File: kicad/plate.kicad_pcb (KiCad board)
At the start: 2 copper layers, 123.5 x 85.3 mm, 22 parts, among them J1 TRRS, SW10 SW_PUSH, SW11 SW_PUSH, SW12 SW_PUSH, SW14 SW_PUSH, SW15 SW_PUSH, SW16 SW_PUSH, SW17 SW_PUSH, SW18 SW_PUSH, SW2 SW_PUSH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

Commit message: Plate build
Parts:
- SW10, SW11, SW12, SW14, SW15, SW16, SW17, SW18, SW2, SW20, SW21, SW3, SW4, SW5, SW6, SW8, SW9: footprint chocs:SW_PG1350_reversible_b2 -> broom:SW_PG1350_cut
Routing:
- net (no net): track 1542.1 -> 0.00 mm, vias 9 -> 0
- removed copper zone on B.Cu, net (none)
- removed copper zone on F.Cu, net (none)

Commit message: Plate ready
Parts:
- removed J1: TRRS, broom:TRRS-PJ-DPB2
- removed RSW1: Val**, foostan:ResetSW
- removed U1: ProMicro, broom:ProMicro_v2
- removed h2 (x2): h2, chocorne:LEGO_HOLE
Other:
- outline, holes or cut-outs redrawn

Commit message: pm cover
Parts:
- added h2: h2, chocorne:LEGO_HOLE, F.Cu at (197.3, 109.0)
- added h2: h2, chocorne:LEGO_HOLE, F.Cu at (212.6, 109.0)
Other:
- board size 123.5 x 85.3 mm -> 126.8 x 85.3 mm
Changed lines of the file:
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@@
     (fp_line (start -7 -7) (end 7 -7) (layer "Edge.Cuts") (width 0.15))
+  )
+  (footprint "chocorne:LEGO_HOLE" (layer "F.Cu")
+    (at 197.322 108.987)
+    (descr "Mounting Hole 2.2mm, no annular, M2")
+    (tags "mounting hole 2.2mm no annular m2")
+    (attr exclude_from_pos_files exclude_from_bom)
+    (fp_text reference "h2" (at 0 -3.2) (layer "F.SilkS") hide
+      (effects (font (size 1 1) (thickness 0.15)))
+    )
+    (fp_text value "h2" (at 0 3.2) (layer "F.Fab")
+      (effects (font (size 1 1) (thickness 0.15)))
+    )
+    (fp_text user "${REFERENCE}" (at 0.3 0) (layer "F.Fab")
+      (effects (font (size 1 1) (thickness 0.15)))
+    )
+    (fp_circle (center 0 0) (end 1.2 0) (layer "Cmts.User") (width 0.15) (fill none))
+    (fp_circle (center 0 0) (end 1.2 0) (layer "F.CrtYd") (width 0.05) (fill none))
+    (pad "h2" thru_hole circle locked (at 0 0) (size 2.4 2.4) (drill 2.2) (layers *.Cu *.Mask))
   )
   (footprint "broom:SW_PG1350_cut" (layer "F.Cu")
@@
     (fp_line (start -7 7) (end 7 7) (layer "Edge.Cuts") (width 0.15))
     (fp_line (start 7 7) (end 7 -7) (layer "Edge.Cuts") (width 0.15))
+  )
+  (footprint "chocorne:LEGO_HOLE" (layer "F.Cu")
+    (at 212.567 108.982)
+    (descr "Mounting Hole 2.2mm, no annular, M2")
+    (tags "mounting hole 2.2mm no annular m2")
+    (attr exclude_from_pos_files exclude_from_bom)
+    (fp_text reference "h2" (at 0 -3.2) (layer "F.SilkS") hide
+      (effects (font (size 1 1) (thickness 0.15)))
+    )
+    (fp_text value "h2" (at 0 3.2) (layer "F.Fab")
+      (effects (font (size 1 1) (thickness 0.15)))
+    )
+    (fp_text user "${REFERENCE}" (at 0.3 0) (layer "F.Fab")
+      (effects (font (size 1 1) (thickness 0.15)))
+    )
+    (fp_circle (center 0 0) (end 1.2 0) (layer "Cmts.User") (width 0.15) (fill none))
+    (fp_circle (center 0 0) (end 1.2 0) (layer "F.CrtYd") (width 0.05) (fill none))
+    (pad "h2" thru_hole circle locked (at 0 0) (size 2.4 2.4) (drill 2.2) (layers *.Cu *.Mask))
   )
   (footprint "broom:SW_PG1350_cut" (layer "F.Cu")
@@
   )
   (gr_arc (start 189.869405 63.084258) (end 190.664405 63.059258) (angle -75.82503188) (layer "Edge.Cuts") (width 0.15))
+  (gr_line (start 194.086 72.697) (end 214.538 72.697) (layer "Edge.Cuts") (width 0.15))
   (gr_line (start 211.234 117.98) (end 211.231003 128.040862) (layer "Edge.Cuts") (width 0.15))
   (gr_line (start 190.669 118) (end 190.664405 63.059258) (layer "Edge.Cuts") (width 0.15))
+  (gr_line (start 194.123 111.275) (end 214.538 111.262) (layer "Edge.Cuts") (width 0.15))
   (gr_line (start 88.127953 83.292666) (end 105.361412 136.251738) (layer "Edge.Cuts") (width 0.15))
+  (gr_line (start 194.086 111.262) (end 194.086 72.697) (layer "Edge.Cuts") (width 0.15))
   (gr_arc (start 155.4857 240.406359) (end 190.039849 62.307342) (angle -30.52241692) (layer "Edge.Cuts") (width 0.15))
   (gr_arc (start 188.968743 128.55) (end 206.239908 142.606113) (angle -40.45049692) (layer "Edge.Cuts") (width 0.15))
@@
   (gr_arc (start 141.689 320.542281) (end 106.709135 136.975628) (angle 18.02701016) (layer "Edge.Cuts") (width 0.15))
   (gr_arc (start 135.189 334.05) (end 165.233781 135.161726) (angle 10.5566717) (layer "Edge.Cuts") (width 0.15))
+  (gr_line (start 214.538 111.262) (end 214.538 72.697) (layer "Edge.Cuts") (width 0.15))
   (gr_arc (start 202.695496 139.738695) (end 201.163167 144.032518) (angle -70.66711935) (layer "Edge.Cuts") (width 0.15))
   (gr_arc (start 106.46079 135.821466) (end 105.361412 136.251738) (angle -80.76911852) (layer "Edge.Cuts") (width 0.15))

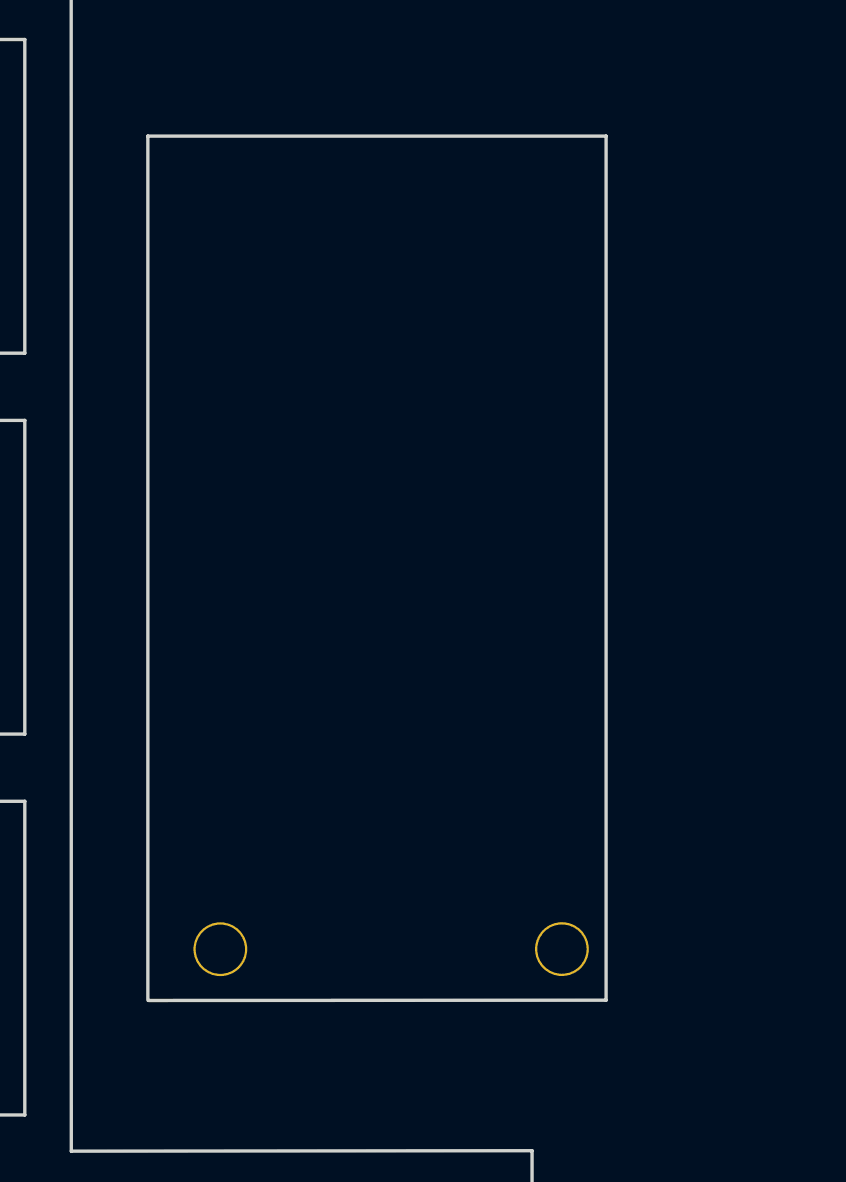
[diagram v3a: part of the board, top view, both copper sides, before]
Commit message: pm cover - mouse bites
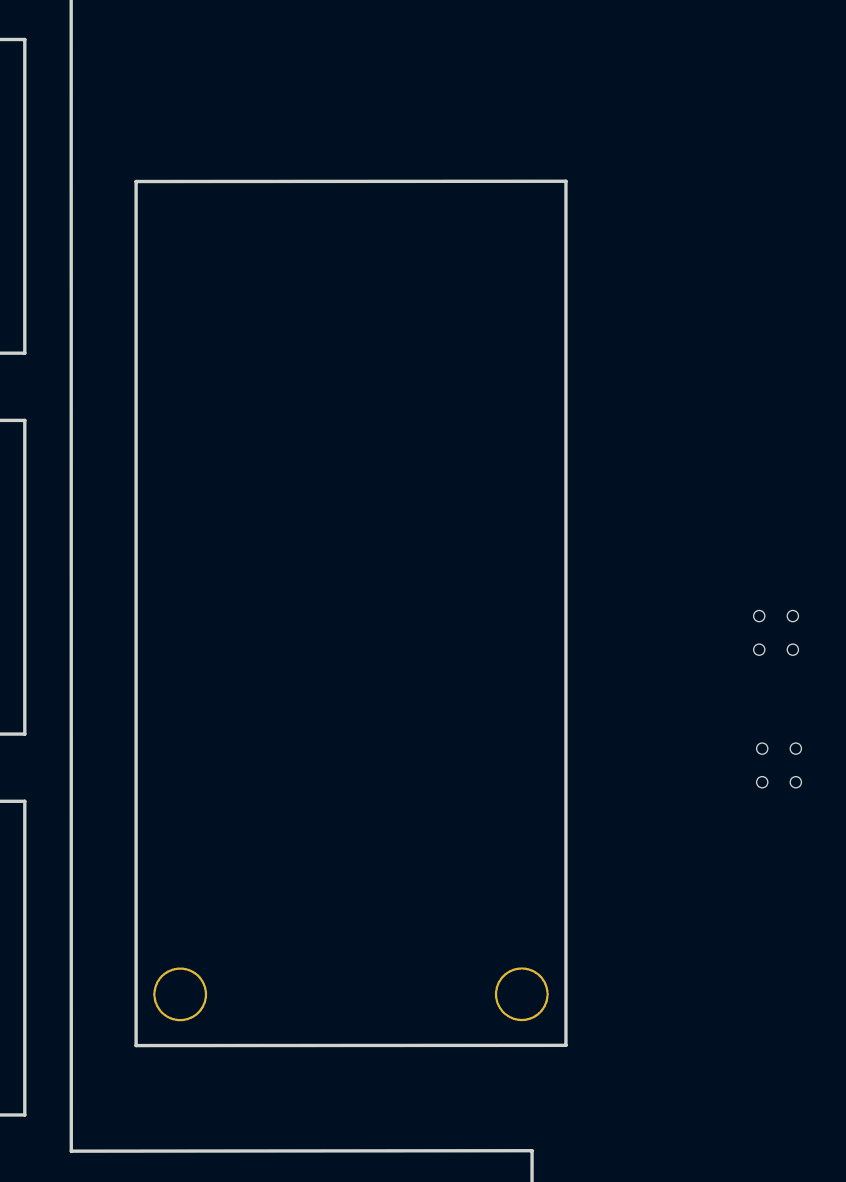
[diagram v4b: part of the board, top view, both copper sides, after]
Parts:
- added REF**: VAL**, broom:mouse-bite-2mm-slot-with-space-for-track, F.Cu at (222.1, 94.9)
- added REF**: VAL**, broom:mouse-bite-2mm-slot-with-space-for-track, F.Cu at (222.3, 100.8)
- moved h2 2.70 mm to (195.5, 111.0)
- moved h2 2.70 mm to (210.8, 111.0)
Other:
- board size 126.8 x 85.3 mm -> 125 x 85.3 mm
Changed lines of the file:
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@@
   )
   (net 0 "")
+  (footprint "broom:mouse-bite-2mm-slot-with-space-for-track" (layer "F.Cu")
+    (at 222.123 94.868 90)
+    (attr exclude_from_pos_files exclude_from_bom)
+    (fp_text reference "REF**" (at 0 -2 90) (layer "F.SilkS") hide
+      (effects (font (size 1 1) (thickness 0.2)))
+    )
+    (fp_text value "VAL**" (at 0 2.1 90) (layer "F.SilkS") hide
+      (effects (font (size 1 1) (thickness 0.2)))
+    )
+    (fp_arc (start -2 0) (end -2 -1) (angle 180) (layer "Dwgs.User") (width 0.1))
+    (fp_arc (start 2 0) (end 2 1) (angle 180) (layer "Dwgs.User") (width 0.1))
+    (fp_circle (center 2 0) (end 2.06 0) (layer "Dwgs.User") (width 0.05) (fill none))
+    (fp_circle (center -2 0) (end -2 -0.06) (layer "Dwgs.User") (width 0.05) (fill none))
+    (fp_line (start 2 0) (end 2 0) (layer "Eco1.User") (width 2))
+    (fp_line (start -2 0) (end -2 0) (layer "Eco1.User") (width 2))
+    (pad "" np_thru_hole circle locked (at -0.75 0.75 90) (size 0.5 0.5) (drill 0.5) (layers *.Cu *.Mask))
+    (pad "" np_thru_hole circle locked (at 0.75 -0.75 90) (size 0.5 0.5) (drill 0.5) (layers *.Cu *.Mask))
+    (pad "" np_thru_hole circle locked (at 0.75 0.75 90) (size 0.5 0.5) (drill 0.5) (layers *.Cu *.Mask))
+    (pad "" np_thru_hole circle locked (at -0.75 -0.75 90) (size 0.5 0.5) (drill 0.5) (layers *.Cu *.Mask))
+  )
   (footprint "broom:SW_PG1350_cut" (layer "F.Cu")
     (at 124.919 93.53 8)
@@
   )
   (footprint "chocorne:LEGO_HOLE" (layer "F.Cu")
-    (at 197.322 108.987)
+    (at 195.53 111.002)
     (descr "Mounting Hole 2.2mm, no annular, M2")
     (tags "mounting hole 2.2mm no annular m2")
@@
     (fp_line (start 7 7) (end 7 -7) (layer "Edge.Cuts") (width 0.15))
   )
+  (footprint "broom:mouse-bite-2mm-slot-with-space-for-track" (layer "F.Cu")
+    (at 222.256 100.784 180)
+    (attr exclude_from_pos_files exclude_from_bom)
+    (fp_text reference "REF**" (at 0 -2) (layer "F.SilkS") hide
+      (effects (font (size 1 1) (thickness 0.2)))
+    )
+    (fp_text value "VAL**" (at 0 2.1) (layer "F.SilkS") hide
+      (effects (font (size 1 1) (thickness 0.2)))
+    )
+    (fp_arc (start -2 0) (end -2 -1) (angle 180) (layer "Dwgs.User") (width 0.1))
+    (fp_arc (start 2 0) (end 2 1) (angle 180) (layer "Dwgs.User") (width 0.1))
+    (fp_circle (center -2 0) (end -2 -0.06) (layer "Dwgs.User") (width 0.05) (fill none))
+    (fp_circle (center 2 0) (end 2.06 0) (layer "Dwgs.User") (width 0.05) (fill none))
+    (fp_line (start -2 0) (end -2 0) (layer "Eco1.User") (width 2))
+    (fp_line (start 2 0) (end 2 0) (layer "Eco1.User") (width 2))
+    (pad "" np_thru_hole circle locked (at 0.75 0.75 180) (size 0.5 0.5) (drill 0.5) (layers *.Cu *.Mask))
+    (pad "" np_thru_hole circle locked (at 0.75 -0.75 180) (size 0.5 0.5) (drill 0.5) (layers *.Cu *.Mask))
+    (pad "" np_thru_hole circle locked (at -0.75 -0.75 180) (size 0.5 0.5) (drill 0.5) (layers *.Cu *.Mask))
+    (pad "" np_thru_hole circle locked (at -0.75 0.75 180) (size 0.5 0.5) (drill 0.5) (layers *.Cu *.Mask))
+  )
   (footprint "chocorne:LEGO_HOLE" (layer "F.Cu")
-    (at 212.567 108.982)
+    (at 210.775 110.997)
     (descr "Mounting Hole 2.2mm, no annular, M2")
     (tags "mounting hole 2.2mm no annular m2")
@@
       (effects (font (size 1 1) (thickness 0.15)))
     )
-    (fp_text value "h2" (at 0 3.2) (layer "F.Fab")
+    (fp_text value "h2" (at -17.16 -2.041) (layer "F.Fab")
       (effects (font (size 1 1) (thickness 0.15)))
     )
@@
   )
   (gr_arc (start 189.869405 63.084258) (end 190.664405 63.059258) (angle -75.82503188) (layer "Edge.Cuts") (width 0.15))
-  (gr_line (start 194.086 72.697) (end 214.538 72.697) (layer "Edge.Cuts") (width 0.15))
+  (gr_line (start 193.562 74.723) (end 212.746 74.712) (layer "Edge.Cuts") (width 0.15))
   (gr_line (start 211.234 117.98) (end 211.231003 128.040862) (layer "Edge.Cuts") (width 0.15))
   (gr_line (start 190.669 118) (end 190.664405 63.059258) (layer "Edge.Cuts") (width 0.15))
-  (gr_line (start 194.123 111.275) (end 214.538 111.262) (layer "Edge.Cuts") (width 0.15))
+  (gr_line (start 193.562 113.288) (end 212.746 113.277) (layer "Edge.Cuts") (width 0.15))
   (gr_line (start 88.127953 83.292666) (end 105.361412 136.251738) (layer "Edge.Cuts") (width 0.15))
-  (gr_line (start 194.086 111.262) (end 194.086 72.697) (layer "Edge.Cuts") (width 0.15))
+  (gr_line (start 193.562 113.288) (end 193.562 74.723) (layer "Edge.Cuts") (width 0.15))
   (gr_arc (start 155.4857 240.406359) (end 190.039849 62.307342) (angle -30.52241692) (layer "Edge.Cuts") (width 0.15))
   (gr_arc (start 188.968743 128.55) (end 206.239908 142.606113) (angle -40.45049692) (layer "Edge.Cuts") (width 0.15))
@@
   (gr_arc (start 141.689 320.542281) (end 106.709135 136.975628) (angle 18.02701016) (layer "Edge.Cuts") (width 0.15))
   (gr_arc (start 135.189 334.05) (end 165.233781 135.161726) (angle 10.5566717) (layer "Edge.Cuts") (width 0.15))
-  (gr_line (start 214.538 111.262) (end 214.538 72.697) (layer "Edge.Cuts") (width 0.15))
+  (gr_line (start 212.746 113.277) (end 212.746 74.712) (layer "Edge.Cuts") (width 0.15))
   (gr_arc (start 202.695496 139.738695) (end 201.163167 144.032518) (angle -70.66711935) (layer "Edge.Cuts") (width 0.15))
   (gr_arc (start 106.46079 135.821466) (end 105.361412 136.251738) (angle -80.76911852) (layer "Edge.Cuts") (width 0.15))
   (gr_line (start 190.669 118) (end 211.234 117.98) (layer "Edge.Cuts") (width 0.15))
+  (group "" (id a308bf8a-7b15-4c69-8d2d-f307d8baa6de)
+    (members
+      2600aef0-55e7-486c-97a5-7d49fb7776f9
+      47053596-ba74-48b3-a822-1d2797a26388
+      60d902c8-7d9d-4d47-ae0f-074e021be140
+      8520a7a4-f90c-4619-9e30-1e98949422c4
+      8a669e94-7038-46fd-9b70-906083bff600
+      e733b390-f7c4-44db-8681-523d96046aea
+    )
+  )
 )
